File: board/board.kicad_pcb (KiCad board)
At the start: 2 copper layers, 45 x 13 mm, 17 parts, among them J1 022_battery_cells, J2 Conn_01x02_Male, J3 003_power, U1 TLV61220

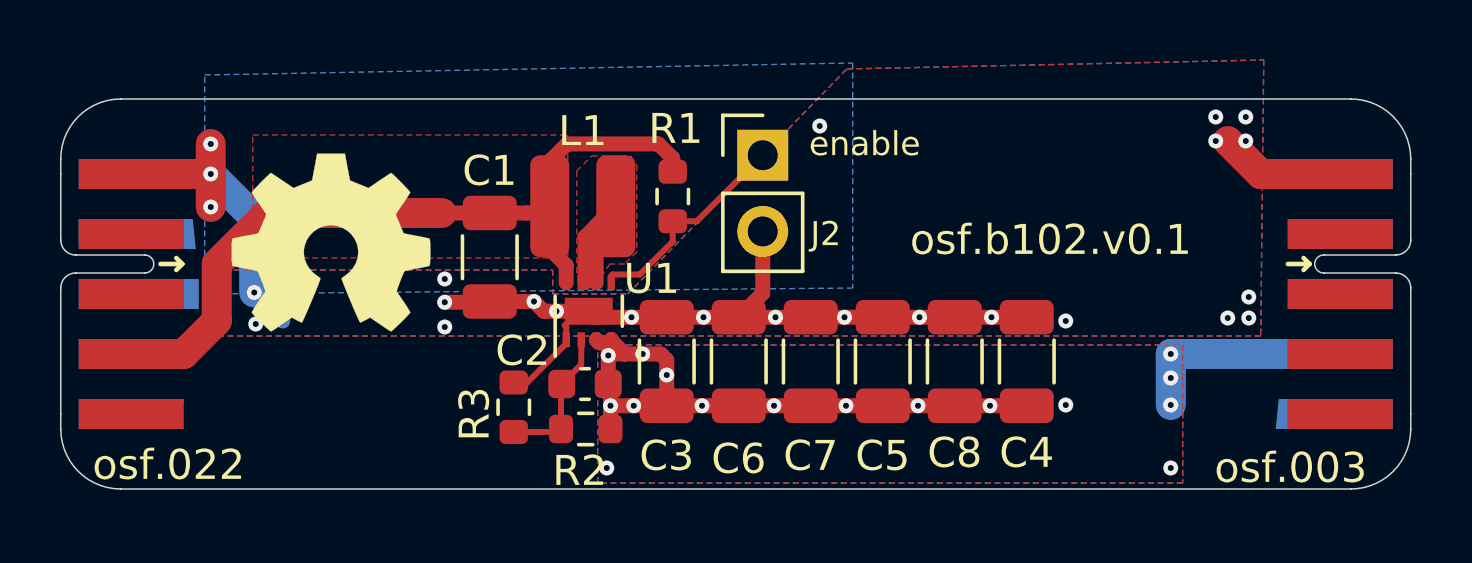
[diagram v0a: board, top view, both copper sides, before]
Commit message: added resistor to allow shorting of bat low to gnd
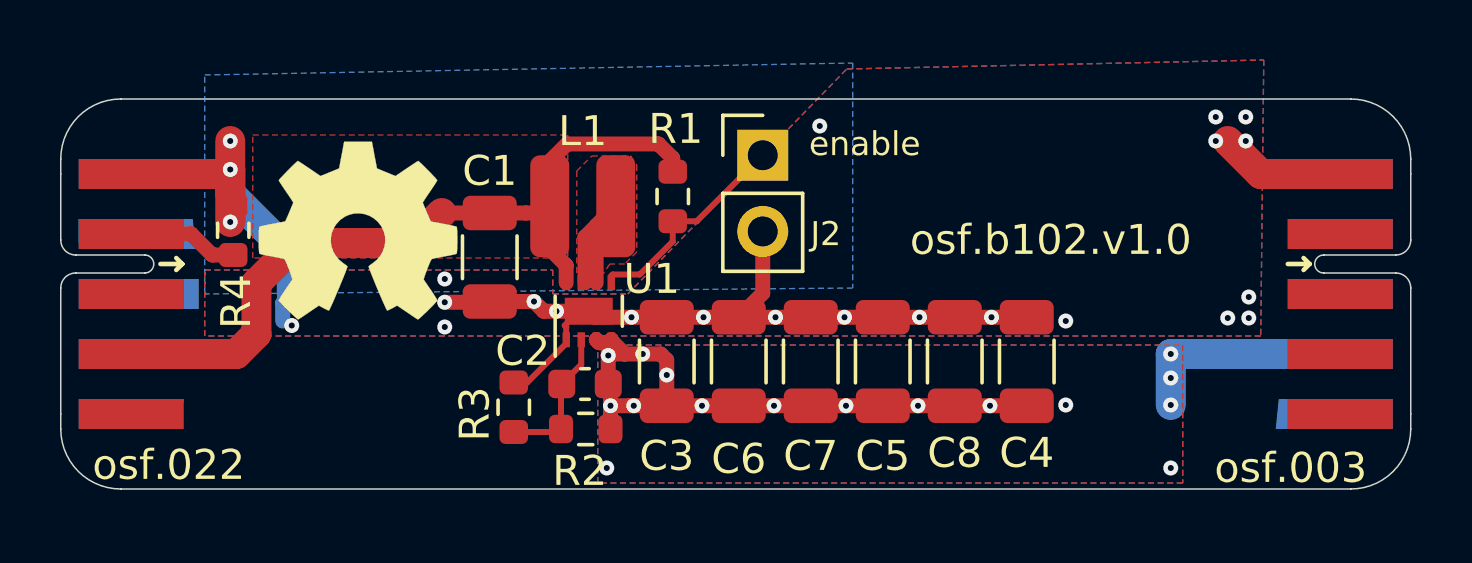
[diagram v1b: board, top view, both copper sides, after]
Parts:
- added R4: d.n.p, Resistor_SMD:R_0603_1608Metric, F.Cu at (145.8, 94.4)
- J2: value Conn_01x02_Male -> d.n.p
- U1: value TLV61220 -> TPS61021A
- moved LOGO1 0.98 mm to (149.9, 94.4)
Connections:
- J1 pad 2: unconnected-(J1-Pad2) -> Net-(J1-Pad2)
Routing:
- net Net-(J1-Pad2): track 0.00 -> 3.69 mm
- net GND: track 41.6 -> 43.0 mm
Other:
- board text added: "osf.b102.v1.0"
- board text removed: "osf.b102.v0.1"

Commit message: added decoupling caps
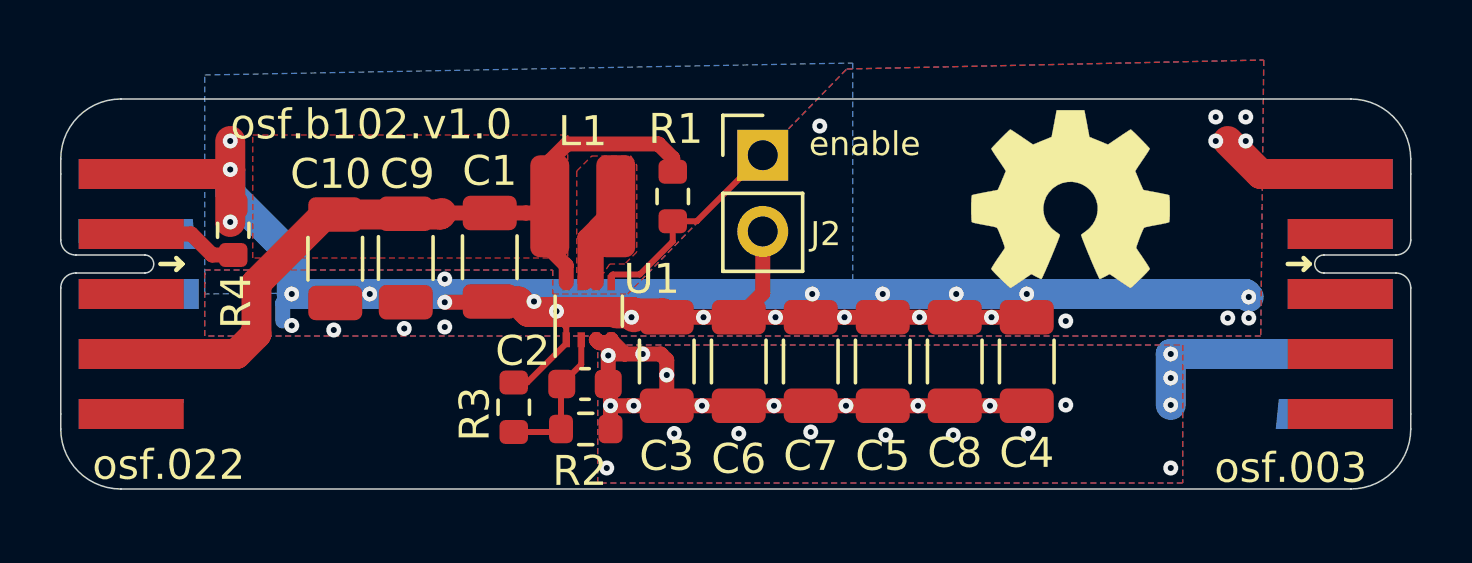
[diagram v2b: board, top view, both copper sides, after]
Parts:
- added C10: 22uF, Capacitor_SMD:C_1206_3216Metric, F.Cu at (149.2, 95.3)
- added C9: 22uF, Capacitor_SMD:C_1206_3216Metric, F.Cu at (151.5, 95.3)
- moved LOGO1 23.8 mm to (173.7, 93.3)
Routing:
- net GND: track 43.0 -> 81.5 mm, vias 25 -> 32
- net /step up/3.3V: vias 16 -> 22
